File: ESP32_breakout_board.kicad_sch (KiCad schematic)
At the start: 12 parts, among them J1 Conn_01x15, J2 Conn_01x15

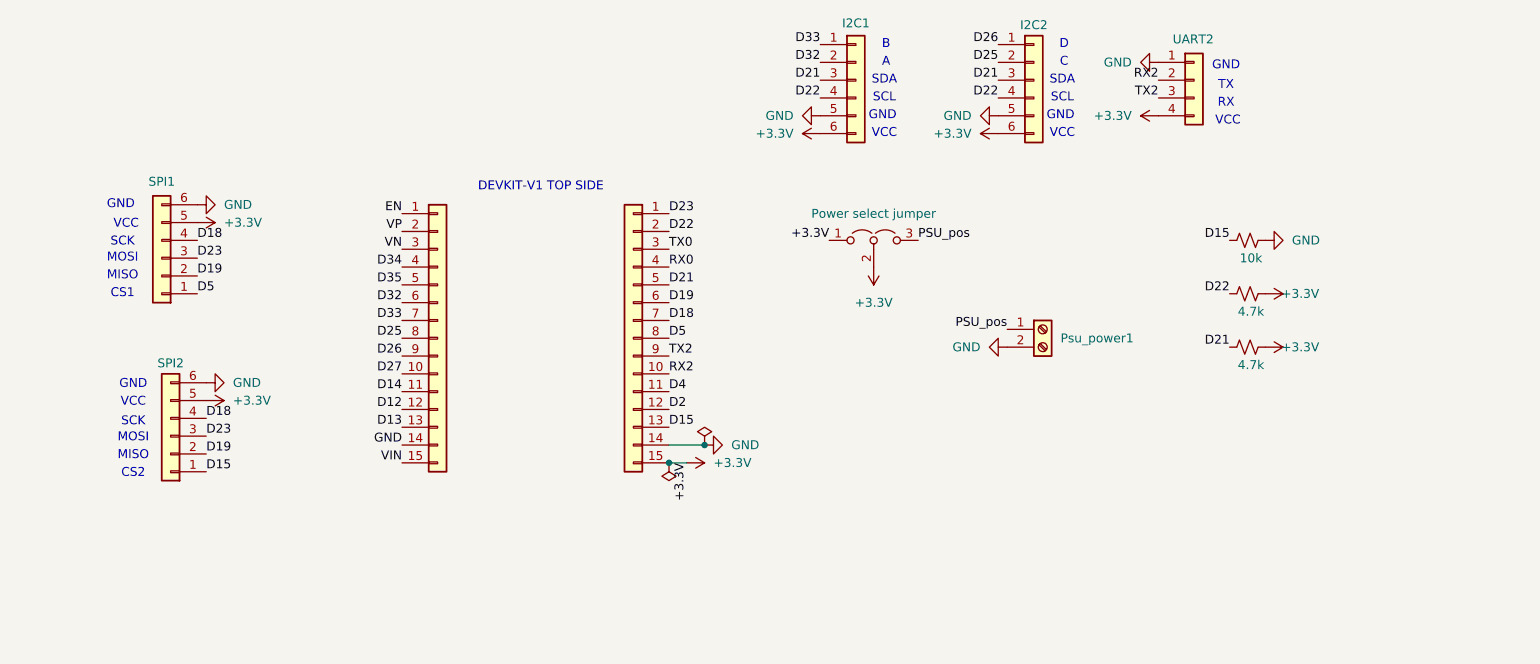
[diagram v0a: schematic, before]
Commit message: changed design
removed the 10k pull down after careful consideration and cleaned up the design a bit
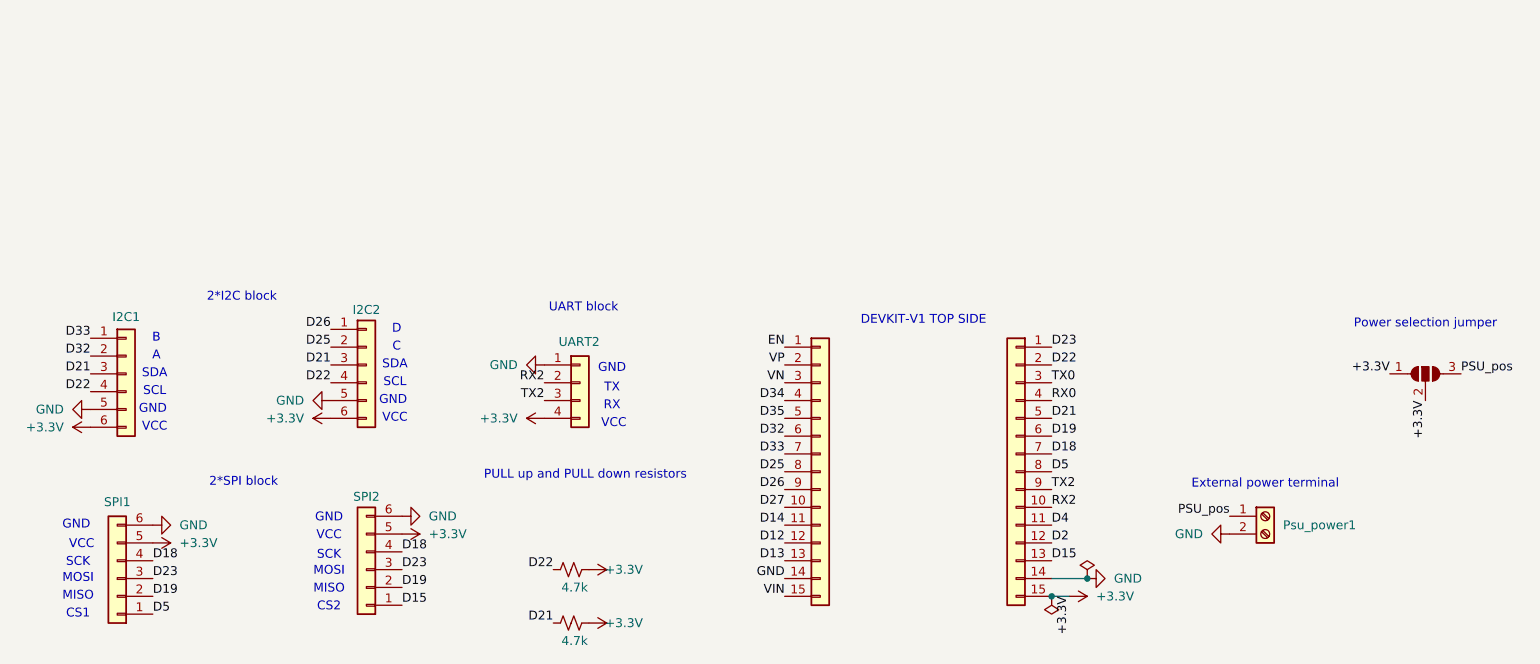
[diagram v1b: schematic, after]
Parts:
- removed JP1: Power select jumper, Connector_PinHeader_2.54mm:PinHeader_1x03_P2.54mm_Vertical, symbol Jumper:Jumper_3_Open
- removed R3: 10k, Resistor_THT:R_Axial_DIN0204_L3.6mm_D1.6mm_P7.62mm_Horizontal, symbol Device:R_Small_US
- added JP2: SolderJumper_3_Open, Jumper:SolderJumper-3_P1.3mm_Open_Pad1.0x1.5mm, symbol Jumper:SolderJumper_3_Open
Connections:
- net +3.3V: now also JP2.1 (A), JP2.2 (C)
- net PSU_pos: now also JP2.3 (B)
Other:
- note added: "2*I2C block"
- note added: "2*SPI block"
- note added: "External power terminal"
- note added: "PULL up and PULL down resistors"
- note added: "Power selection jumper"
- note added: "UART block"
- moved on the sheet: I2C1, I2C2, Psu_power1, SPI1, SPI2, UART2
